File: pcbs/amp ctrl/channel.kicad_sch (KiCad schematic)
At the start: 97 parts, among them J11 Conn_01x02, J6 Conn_02x02, J8 Conn_02x10_Odd_Even, J9 Conn_02x02, J92 Conn_01x02, Q1 MMBT3904, Q2 MMBT3906, Q3 MMBT3904, Q36 MMBT3904, Q37 2N7002, Q4 MMBT3906, U1 INA821/819, U2 OPA37, U3 ADA4004-1, U7 TLVH431, U73 TBD, U9 TLVH431

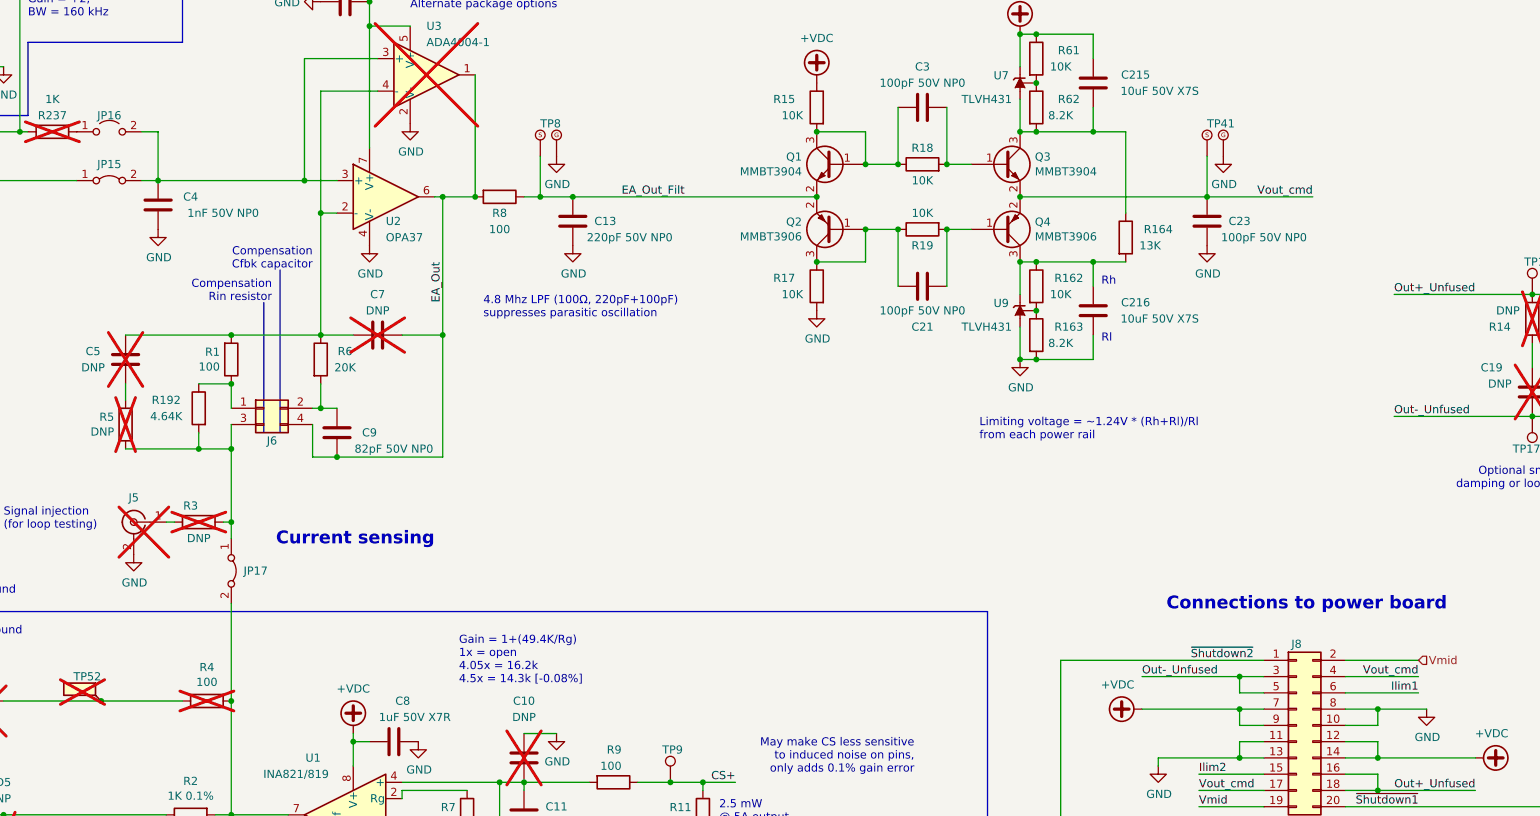
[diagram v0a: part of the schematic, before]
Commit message: Amp ctrl: DAC-filter jumpers, paralleling channels
Added jumpers to disconnect 2nd set of filter capacitors in DAC smoothing filter (fixes #42)
Extended shield footprint around digital section, no longer fits off-the-shelf part (but haven't had a reason to use it yet) to leave room for jumpers
Changed to an experimental channel-paralleling scheme (#19)
Finished copying level shifter layout to other channels (#9)
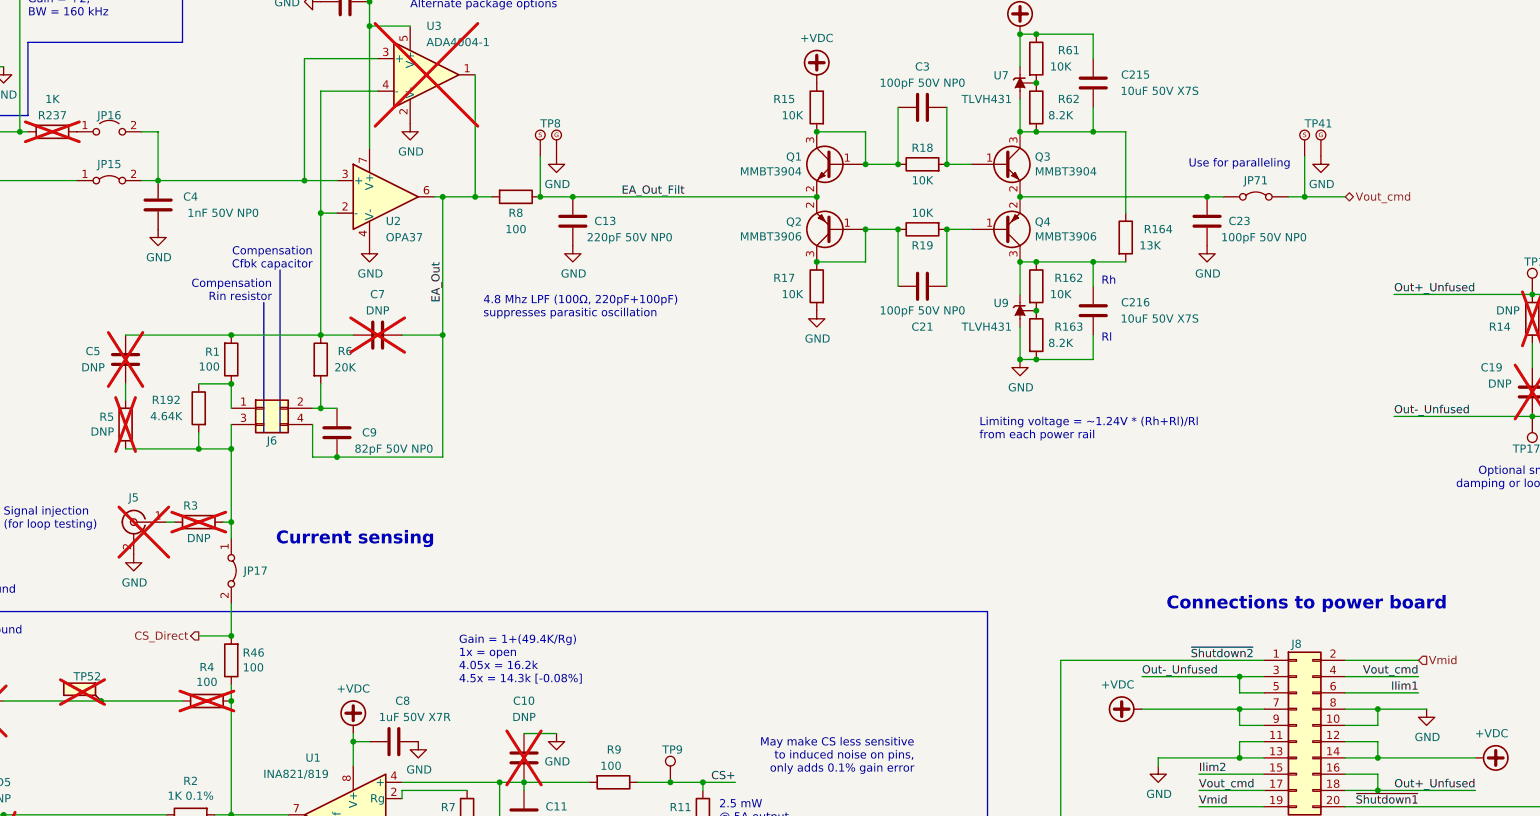
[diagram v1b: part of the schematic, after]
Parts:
- added JP71: Jumper_2_Bridged, Jumper:SolderJumper-2_P1.3mm_Bridged_RoundedPad1.0x1.5mm, symbol Jumper:Jumper_2_Bridged
- added R46: 100, Resistor_SMD:R_0805_2012Metric, symbol Device:R
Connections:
- net Vout_cmd: now also JP71.2 (B); no longer C23.2, Q3.2 (E), Q4.2 (E)
- net at R2.2, R4.2, U1.7: now also R46.1; no longer JP17.2 (B)
- new net: C23.2, JP71.1 (A), Q3.2 (E), Q4.2 (E)
- new net CS_Direct: JP17.2 (B), R46.2
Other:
- note added: "Use for paralleling"
- moved on the sheet: R8, TP41

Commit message: Library & amp ctrl updates for spring connectors
Library: added footprints for spring connector bare pads (both 70AAJ & SIB)
Library: added SIB contact point markers to all footprints
Library: corrected 70AAJ outline size
Amp ctrl: started layout change on channel 2
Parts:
- added J10, J37, J65, J67: Conn_01x05, shim:Conn_70AAJ-M_SIB_1x05_P2.54mm_F_bare, symbol Connector_Generic:Conn_01x05

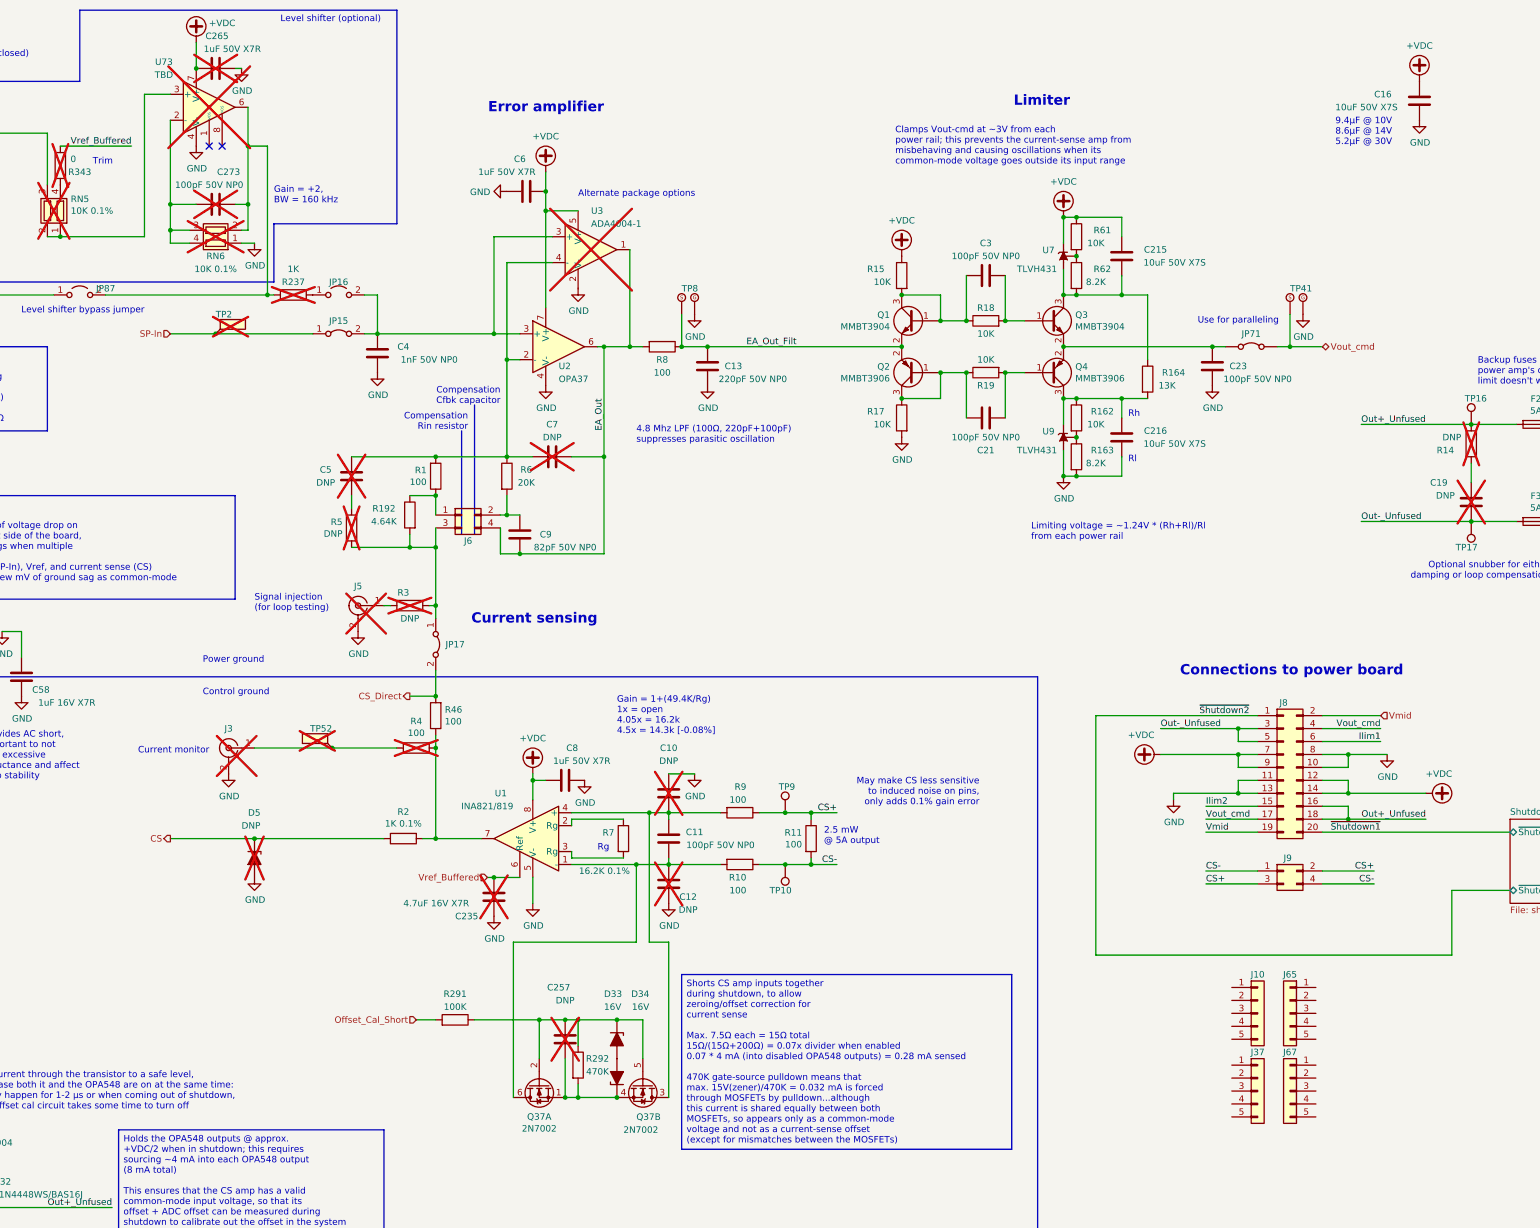
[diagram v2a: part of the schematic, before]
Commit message: Spring connector layout updates
Amp ctrl: added spring connectors for current sense, thermistors, +5V regulator
Amp ctrl: changed pass-through screwdriver holes to mounting holes
Amp ctrl: added part number to optional level shifter
Amp pwr: marked DNP components as DNP
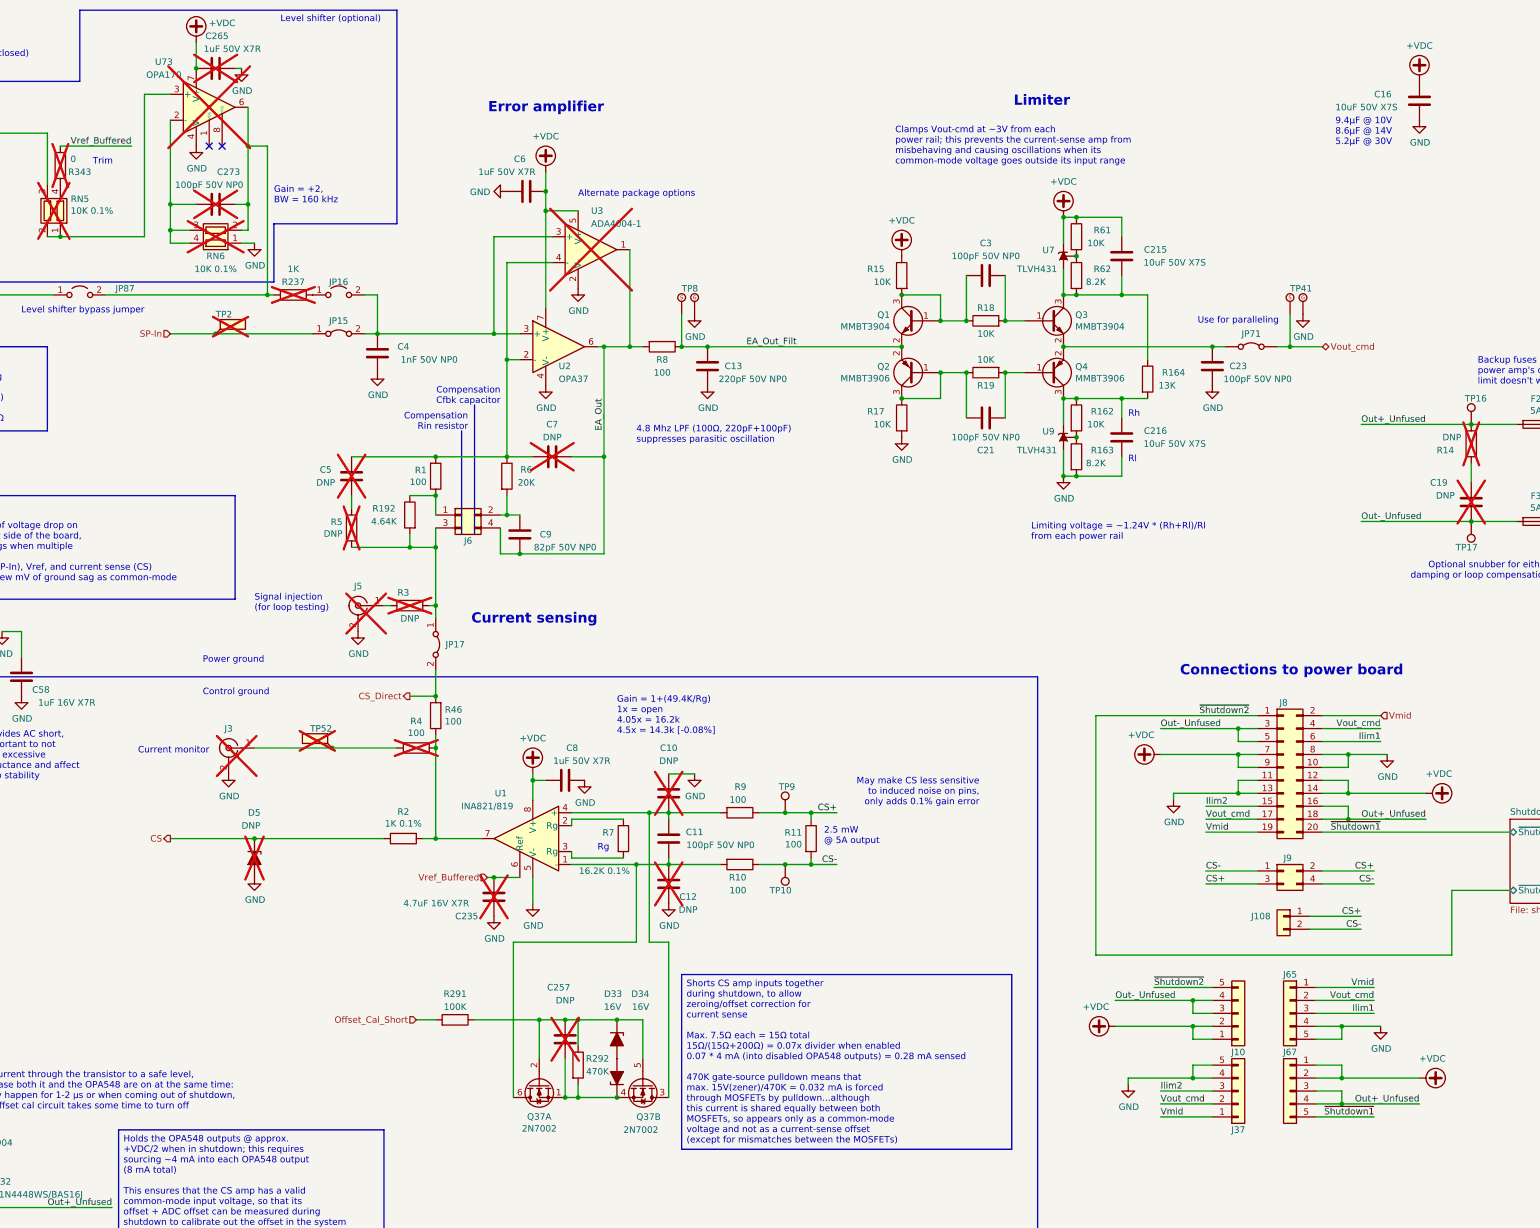
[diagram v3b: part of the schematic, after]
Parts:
- added J108: Conn_01x02, shim:Conn_70AAJ-M_SIB_1x02_P2.54mm_F_bare, symbol Connector_Generic:Conn_01x02
- U3: MPN (none) -> ADA4004-1ARJZ-R7; Manufacturer (none) -> Analog Devices
- U73: value TBD -> OPA170; MPN (none) -> OPA170AIDR; Manufacturer (none) -> Texas Instruments
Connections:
- net +VDC: now also J10.1 (Pin_1), J10.2 (Pin_2), J67.1 (Pin_1), J67.2 (Pin_2)
- net CS+: now also J108.1 (Pin_1)
- net CS-: now also J108.2 (Pin_2)
- net GND: now also J37.4 (Pin_4), J37.5 (Pin_5), J65.4 (Pin_4), J65.5 (Pin_5)
- net Ilim1: now also J65.3 (Pin_3)
- net Ilim2: now also J37.3 (Pin_3)
- net Out+_Unfused: now also J67.3 (Pin_3), J67.4 (Pin_4)
- net Out-_Unfused: now also J10.3 (Pin_3), J10.4 (Pin_4)
- net Vmid: now also J37.1 (Pin_1), J65.1 (Pin_1)
- net Vout_cmd: now also J37.2 (Pin_2), J65.2 (Pin_2)
- net ~{Shutdown1}: now also J67.5 (Pin_5)
- net ~{Shutdown2}: now also J10.5 (Pin_5)
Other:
- moved on the sheet: J10, J37

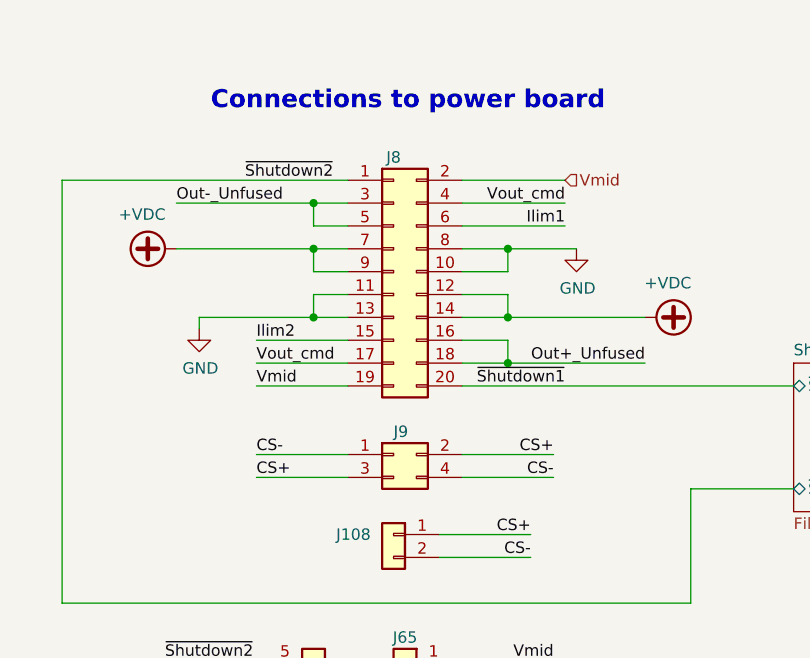
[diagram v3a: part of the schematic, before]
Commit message: Amp ctrl layout for spring pins
Copied layout to all channels & cleaned up inter-channel routing
Updated footprints to latest copies from libraries
Added new SOT-563 footprint for wider clearance between pads, as KiCAD library now has boundary-pushing 0.15 mm (vs. 0.2 mm recc. in 2N7002 datasheet)
Fixed DRC errors
Marked former inter-board connectors (now alternates for spring pins) as DNP
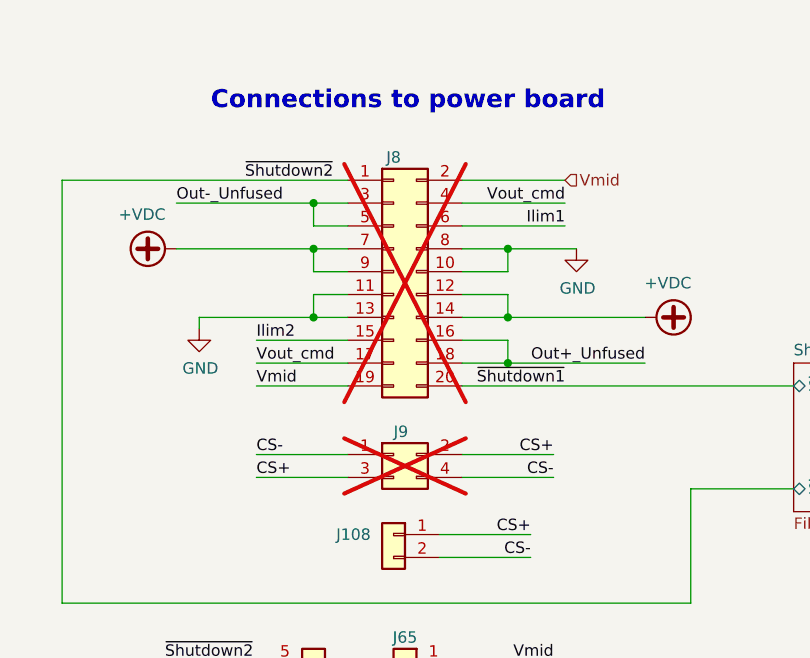
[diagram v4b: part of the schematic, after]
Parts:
- J8, J9: now not fitted
- Q37: footprint Package_TO_SOT_SMD:SOT-563 -> shim:SOT-563
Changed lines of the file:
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@@
 		(on_board yes)
 		(in_pos_files yes)
-		(dnp no)
+		(dnp yes)
 		(property "Reference" "J9"
 			(at 303.53 179.07 0)
@@
 		(on_board yes)
 		(in_pos_files yes)
-		(dnp no)
+		(dnp yes)
 		(property "Reference" "J8"
 			(at 303.53 148.59 0)
@@
 		(in_bom no)
 		(on_board yes)
-		(in_pos_files yes)
+		(in_pos_files no)
 		(dnp no)
 		(property "Reference" "TP8"
@@
 		(in_bom no)
 		(on_board yes)
-		(in_pos_files yes)
+		(in_pos_files no)
 		(dnp no)
 		(property "Reference" "TP9"
@@
 		(in_bom no)
 		(on_board yes)
-		(in_pos_files yes)
+		(in_pos_files no)
 		(dnp no)
 		(property "Reference" "TP10"
@@
 		(in_bom no)
 		(on_board yes)
-		(in_pos_files yes)
+		(in_pos_files no)
 		(dnp no)
 		(property "Reference" "JP20"
@@
 		(in_bom no)
 		(on_board yes)
-		(in_pos_files yes)
+		(in_pos_files no)
 		(dnp no)
 		(property "Reference" "JP15"
@@
 		(in_bom no)
 		(on_board yes)
-		(in_pos_files yes)
+		(in_pos_files no)
 		(dnp no)
 		(property "Reference" "JP16"
@@
 		(in_bom no)
 		(on_board yes)
-		(in_pos_files yes)
+		(in_pos_files no)
 		(dnp no)
 		(property "Reference" "JP17"
@@
 		(in_bom no)
 		(on_board yes)
-		(in_pos_files yes)
+		(in_pos_files no)
 		(dnp no)
 		(property "Reference" "JP18"
@@
 		(in_bom no)
 		(on_board yes)
-		(in_pos_files yes)
+		(in_pos_files no)
 		(dnp no)
 		(property "Reference" "JP19"
@@
 		(in_bom no)
 		(on_board yes)
-		(in_pos_files yes)
+		(in_pos_files no)
 		(dnp no)
 		(property "Reference" "TP16"
@@
 		(in_bom no)
 		(on_board yes)
-		(in_pos_files yes)
+		(in_pos_files no)
 		(dnp no)
 		(property "Reference" "TP17"
@@
 		(in_bom no)
 		(on_board yes)
-		(in_pos_files yes)
+		(in_pos_files no)
 		(dnp no)
 		(property "Reference" "TP41"
@@
 			)
 		)
-		(property "Footprint" "Package_TO_SOT_SMD:SOT-563"
+		(property "Footprint" "shim:SOT-563"
 			(at 177.8 228.6 0)
 			(hide yes)
@@
 			)
 		)
-		(property "Footprint" "Package_TO_SOT_SMD:SOT-563"
+		(property "Footprint" "shim:SOT-563"
 			(at 157.48 228.6 0)
 			(hide yes)
@@
 		(in_bom no)
 		(on_board yes)
-		(in_pos_files yes)
+		(in_pos_files no)
 		(dnp no)
 		(property "Reference" "JP87"
@@
 		(in_bom no)
 		(on_board yes)
-		(in_pos_files yes)
+		(in_pos_files no)
 		(dnp no)
 		(property "Reference" "JP76"
